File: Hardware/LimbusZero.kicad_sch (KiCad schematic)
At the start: 17 parts, among them J1 Conn_01x05, J2 USB_B_Micro, J3 Conn_01x10, J4 Conn_01x10, U1 AMS1117-3.3, U2 M24C01-FMN, U3 STM32C031K6T6

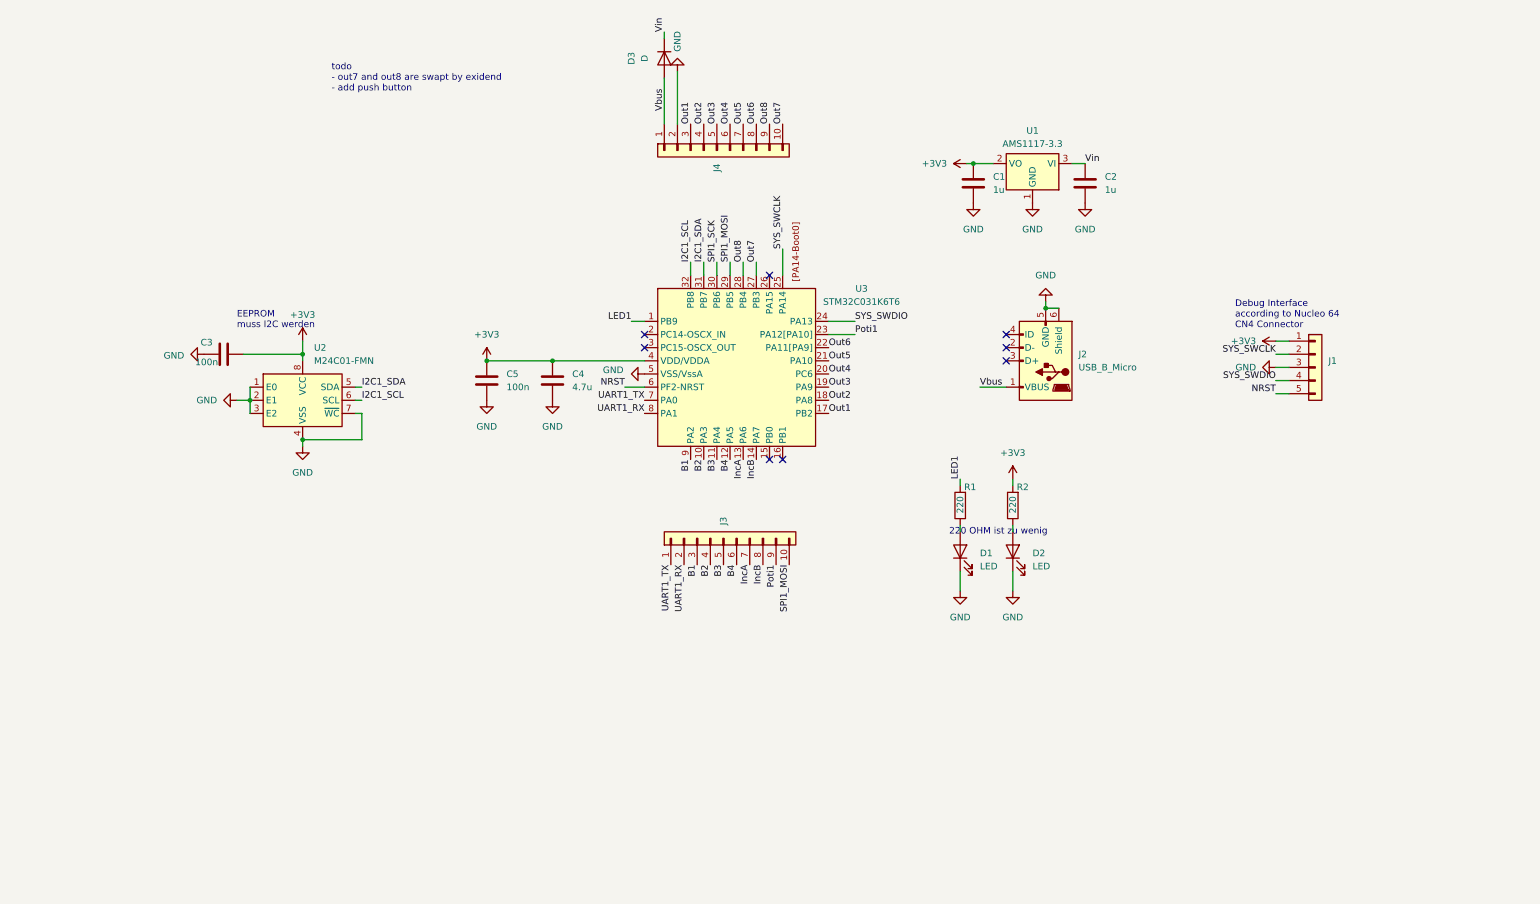
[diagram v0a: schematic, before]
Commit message: started work on version with  C092
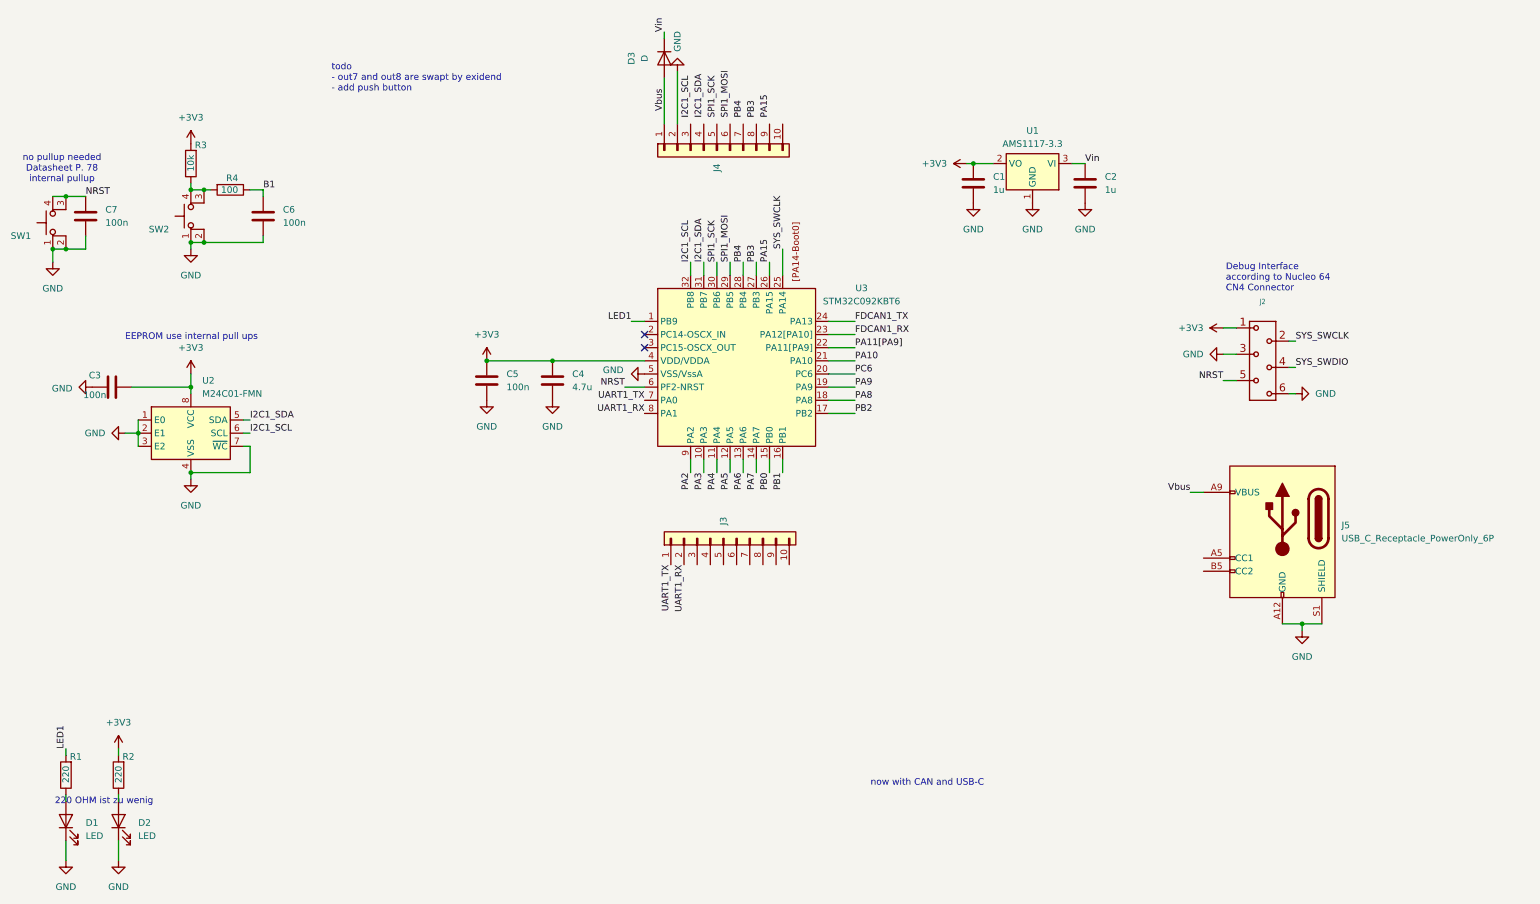
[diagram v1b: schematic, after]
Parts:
- removed J1: Conn_01x05, Connector_PinHeader_2.54mm:PinHeader_1x05_P2.54mm_Horizontal, symbol Connector_Generic:Conn_01x05
- removed J2: USB_B_Micro, Connector_USB:USB_Mini-B_Lumberg_2486_01_Horizontal, symbol Connector:USB_B_Micro
- removed U3: STM32C031K6T6, Package_QFP:LQFP-32_7x7mm_P0.8mm, symbol LWMB_footprints:STM32C031K6T6
- added C6, C7: 100n, Capacitor_SMD:C_0805_2012Metric, symbol Device:C
- added J2: ~, Eagle_WR-WST (rev19b):490107670612_DEBUGGING, symbol WE-SKEDD_WR-WST(rev19b):490107670612_DEBUGGING
- added J5: USB_C_Receptacle_PowerOnly_6P, Connector_USB:USB_C_Receptacle_GCT_USB4125-xx-x-0190_6P_TopMnt_Horizontal, symbol Connector:USB_C_Receptacle_PowerOnly_6P
- added R3: 10k, Resistor_SMD:R_0805_2012Metric, symbol Device:R
- added R4: 100, Resistor_SMD:R_0805_2012Metric, symbol Device:R
- added SW1, SW2: SW_MEC_5E, LMWB_footprints:430181038816, symbol Switch:SW_MEC_5E
- added U3: STM32C092KBT6, Package_QFP:LQFP-32_7x7mm_P0.8mm, symbol LWMB_footprints:STM32C092KBT6
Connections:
- net +3V3: now also J2.1, R3.2, U3.4 (VDD/VDDA)
- net B1: now also C6.1, R4.1; no longer J3.3 (Pin_3)
- net GND: now also C6.2, C7.2, J2.3, J2.6, J5.A12 (GND), J5.B12 (GND), J5.S1 (SHIELD), SW1.1, SW1.2, SW2.1, SW2.2, U3.5 (VSS/VssA)
- net I2C1_SCL: now also U3.32 (PB8)
- net I2C1_SDA: now also U3.31 (PB7)
- net LED1: now also U3.1 (PB9)
- net NRST: now also C7.1, J2.5, SW1.3 (K), SW1.4 (A), U3.6 (PF2-NRST)
- net SPI1_MOSI: now also U3.29 (PB5); no longer J3.10 (Pin_10)
- net SPI1_SCK: now also U3.30 (PB6)
- net SYS_SWCLK: now also J2.2, U3.25 (PA14)
- net SYS_SWDIO: now also J2.4
- net UART1_RX: now also U3.8 (PA1)
- net UART1_TX: now also U3.7 (PA0)
- net Vbus: now also J5.A9 (VBUS), J5.B9 (VBUS)
- net B2: no longer names the net of J3.4 (Pin_4)
- net B3: no longer names the net of J3.5 (Pin_5)
- net B4: no longer names the net of J3.6 (Pin_6)
- net IncA: no longer names the net of J3.7 (Pin_7)
- net IncB: no longer names the net of J3.8 (Pin_8)
- net Out1: no longer names the net of J4.3 (Pin_3)
- net Out2: no longer names the net of J4.4 (Pin_4)
- net Out3: no longer names the net of J4.5 (Pin_5)
- net Out4: no longer names the net of J4.6 (Pin_6)
- net Out5: no longer names the net of J4.7 (Pin_7)
- net Out6: no longer names the net of J4.8 (Pin_8)
- net Out7: no longer names the net of J4.10 (Pin_10)
- net Out8: no longer names the net of J4.9 (Pin_9)
- net Poti1: no longer names the net of J3.9 (Pin_9)
- new net: R3.1, R4.2, SW2.3 (K), SW2.4 (A)
- new net FDCAN1_RX: U3.23 (PA12[PA10])
- new net FDCAN1_TX: U3.24 (PA13)
- new net PA10: U3.21 (PA10)
- new net PA11[PA9]: U3.22 (PA11[PA9])
- new net PA15: U3.26 (PA15)
- new net PA2: U3.9 (PA2)
- new net PA3: U3.10 (PA3)
- new net PA4: U3.11 (PA4)
- new net PA5: U3.12 (PA5)
- new net PA6: U3.13 (PA6)
- new net PA7: U3.14 (PA7)
- new net PA8: U3.18 (PA8)
- new net PA9: U3.19 (PA9)
- new net PB0: U3.15 (PB0)
- new net PB1: U3.16 (PB1)
- new net PB2: U3.17 (PB2)
- new net PB3: U3.27 (PB3)
- new net PB4: U3.28 (PB4)
- new net PC6: U3.20 (PC6)
- no-connect marks 8 -> 2
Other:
- note added: "EEPROM use internal pull ups"
- note added: "no pullup needed Datasheet P. 78 internal pullup"
- note added: "now with CAN and USB-C"
- note removed: "EEPROM muss I2C werden"
- moved on the sheet: C3, D1, D2, R1, R2, U2
